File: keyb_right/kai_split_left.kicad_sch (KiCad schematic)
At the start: 70 parts, among them J1 USB_C_Receptacle_USB2.0, SW1 SW_Push, U2 ATmega32U4-A, Y1 16MHz

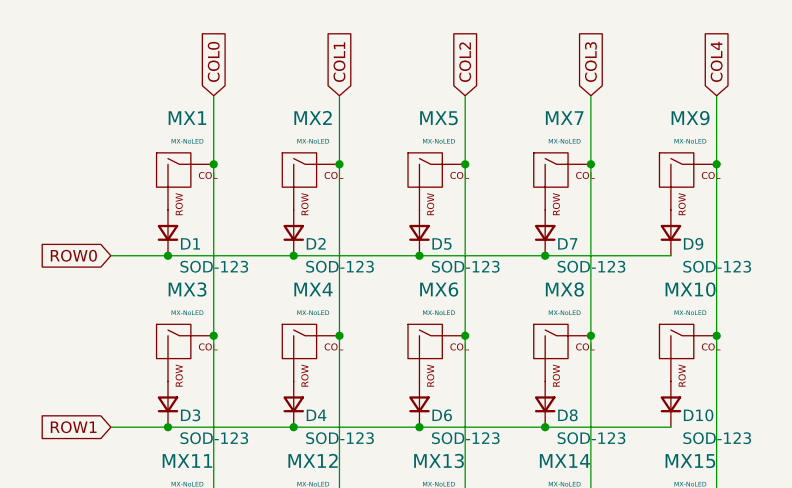
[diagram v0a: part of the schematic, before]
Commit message: Left side only - assigned footprints
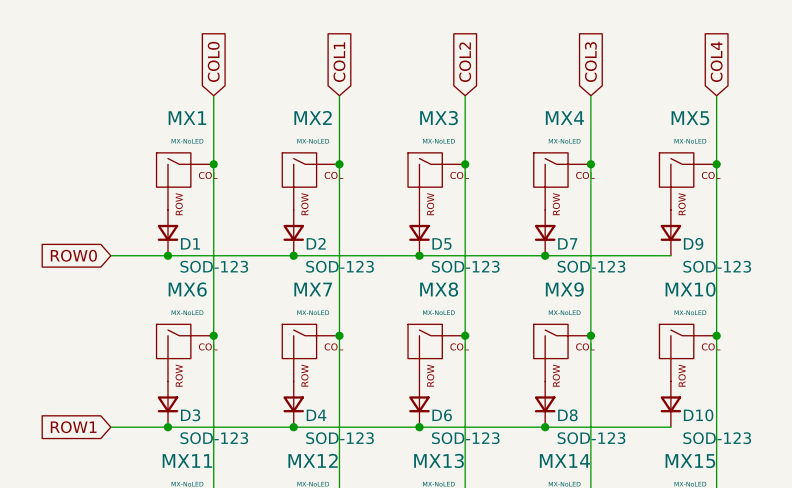
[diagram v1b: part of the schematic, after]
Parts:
- C1, C2, C3, C4, C5, C6, C7: footprint (none) -> Capacitor_SMD:C_0805_2012Metric
- D1, D10, D11, D12, D13, D14, D15, D16, D17, D18, D19, D2, D20, D21, D22, D23, D24, D25, D3, D4, D5, D6, D7, D8, D9: footprint (none) -> Diode_SMD:D_SOD-123
- F1, J1, MX1, MX10, MX11, MX12, MX13, MX14, MX15, MX16, MX17, MX18, MX19, MX2, MX20, MX21, MX22, MX23, MX24, MX25: footprint (none) -> MX_Alps_Hybrid:MX-1U-NoLED
- MX3: renamed from MX5; footprint (none) -> MX_Alps_Hybrid:MX-1U-NoLED
- MX4: renamed from MX7; footprint (none) -> MX_Alps_Hybrid:MX-1U-NoLED
- MX5: renamed from MX9; footprint (none) -> MX_Alps_Hybrid:MX-1U-NoLED
- MX6: renamed from MX3; footprint (none) -> MX_Alps_Hybrid:MX-1U-NoLED
- MX7: renamed from MX4; footprint (none) -> MX_Alps_Hybrid:MX-1U-NoLED
- MX8: renamed from MX6; footprint (none) -> MX_Alps_Hybrid:MX-1U-NoLED
- MX9: renamed from MX8; footprint (none) -> MX_Alps_Hybrid:MX-1U-NoLED
- R1, R2, R3, R4, R5, R6, R7, R8: footprint (none) -> Resistor_SMD:R_0805_2012Metric
- SW1: footprint (none) -> random-keyboard-parts:SKQG-1155865
- Y1: footprint (none) -> Crystal:Crystal_SMD_3225-4Pin_3.2x2.5mm

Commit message: added another library
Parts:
- added J2: AudioJack4, symbol Connector_Audio:AudioJack4
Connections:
- net GND: now also J2.S
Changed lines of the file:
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@@
+    (stroke (width 0) (type default))
+  )
+  (wire (pts (xy 30.48 74.93) (xy 39.37 74.93))
     (stroke (width 0) (type default))
   )
@@
     )
   )
+  (symbol (lib_id "Connector_Audio:AudioJack4") (at 25.4 77.47 0) (unit 1)
+    (in_bom yes) (on_board yes) (dnp no) (fields_autoplaced)
+    (property "Reference" "J2" (at 22.86 69.85 0)
+      (effects (font (size 1.27 1.27)))
+    )
+    (property "Value" "AudioJack4" (at 22.86 72.39 0)
+      (effects (font (size 1.27 1.27)))
+    )
+    (property "Footprint" "" (at 25.4 77.47 0)
+      (effects (font (size 1.27 1.27)) hide)
+    )
+    (property "Datasheet" "~" (at 25.4 77.47 0)
+      (effects (font (size 1.27 1.27)) hide)
+    )
+    (pin "R1")
+    (pin "R2")
+    (pin "S")
+    (pin "T")
+    (instances
+      (project "kai_split_left"
+        (path "/41aeb534-8a24-4ab5-8ab1-e8c232b2e0bb"
+          (reference "J2") (unit 1)
+        )
+      )
+    )
+  )
   (symbol (lib_id "power:GND") (at 48.26 78.74 0) (unit 1)
     (in_bom yes) (on_board yes) (dnp no)
@@
         )
       )
+    )
+  )
+  (symbol (lib_id "power:GND") (at 39.37 74.93 0) (unit 1)
+    (in_bom yes) (on_board yes) (dnp no) (fields_autoplaced)
+    (property "Reference" "#PWR015" (at 39.37 81.28 0)
+      (effects (font (size 1.27 1.27)) hide)
+    )
+    (property "Value" "GND" (at 39.37 80.01 0)
+      (effects (font (size 1.27 1.27)))
+    )
+    (property "Footprint" "" (at 39.37 74.93 0)
+      (effects (font (size 1.27 1.27)) hide)
+    )
+    (property "Datasheet" "" (at 39.37 74.93 0)
+      (effects (font (size 1.27 1.27)) hide)
+    )
+    (pin "1")
+    (instances
+      (project "kai_split_left"
+        (path "/41aeb534-8a24-4ab5-8ab1-e8c232b2e0bb"
+          (reference "#PWR015") (unit 1)
+        )
+      )
